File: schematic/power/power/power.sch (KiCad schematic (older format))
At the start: 9 parts

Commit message: full bridge amplifier schematic
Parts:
- removed C? (x2): C, symbol Device:C
- removed Q? (x2): Q_NMOS_GDS, symbol Device:Q_NMOS_GDS
- removed U? (x2): IR21834, symbol Driver_FET:IR21834
- added C1, C2, C5, C6: C, symbol Device:C
- added C? (x2): CP1, symbol Device:CP1
- added D1, D2: DIODE, symbol pspice:DIODE
- added IC1, IC2: NCP5111PG, DIP794W56P254L959H533Q8N, symbol NCP5111PG:NCP5111PG
- added Q3, Q4: Q_NMOS_GDS, symbol Device:Q_NMOS_GDS
- gave numbers to parts that had none: 3
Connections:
- net labels added: +15V, GND, OUT+, OUT-, PWM_IN, VDD
- wire segments 0 -> 74
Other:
- moved on the sheet: Q1, Q2, U1A

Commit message: Added connectors and filter section
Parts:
- removed U1: 74LS04, symbol 74xx:74LS04
- added C? (x3): C, symbol Device:C
- added J? (x2): Conn_01x04_Female, TerminalBlock_TE-Connectivity:TerminalBlock_TE_282834-4_1x04_P2.54mm_Horizontal, symbol Connector:Conn_01x04_Female
- added J?: Conn_01x02_Female, TerminalBlock_TE-Connectivity:TerminalBlock_TE_282834-2_1x02_P2.54mm_Horizontal, symbol Connector:Conn_01x02_Female
- added L? (x2): INDUCTOR, symbol pspice:INDUCTOR
- IC1, IC2: symbol NCP5111PG:NCP5111PG -> power-rescue:NCP5111PG-NCP5111PG
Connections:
- net +15V: now also J?.2 (Pin_2)
- net GND: now also C?.1, C?.1, J?.3 (Pin_3), J?.3 (Pin_3), J?.4 (Pin_4), J?.4 (Pin_4)
- net VDD: now also J?.1 (Pin_1)
- net PWM-: now reaches IC2.2 (IN)
- net PWM-: now also J?.2 (Pin_2)
- net OUT+ renamed P+
- net P+: now also L?.1
- net OUT- renamed P-
- net P-: now also L?.2
- net PWM_IN renamed PWM+
- net PWM+: now also J?.1 (Pin_1)
- new net O+: C?.2, C?.2, J?.1 (Pin_1), L?.2
- new net O-: C?.1, C?.2, J?.2 (Pin_2), L?.1
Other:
- note added: "Filter Section"
- note added: "Power Section"
- moved on the sheet: C1, C2, C5, C6, C?, D1, D2, IC1, IC2, Q1, Q2, Q3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

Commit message: assign part number to power schematic
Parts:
- removed C2, C5, C6, C? (x3): C, symbol Device:C
- removed C?: CP1, symbol Device:CP1
- removed D1, D2: DIODE, symbol pspice:DIODE
- removed IC2: NCP5111PG, DIP794W56P254L959H533Q8N, symbol power-rescue:NCP5111PG-NCP5111PG
- removed J? (x2): Conn_01x04_Female, TerminalBlock_TE-Connectivity:TerminalBlock_TE_282834-4_1x04_P2.54mm_Horizontal, symbol Connector:Conn_01x04_Female
- removed J?: Conn_01x02_Female, TerminalBlock_TE-Connectivity:TerminalBlock_TE_282834-2_1x02_P2.54mm_Horizontal, symbol Connector:Conn_01x02_Female
- removed L? (x2): INDUCTOR, symbol pspice:INDUCTOR
- added C1, C3, C5, C6, C8: ECE-A1HN100U, Capacitor_THT:CP_Radial_D6.3mm_P2.50mm, symbol Device:CP1
- added C7: UKZ1H101MHM1TO, Capacitor_THT:CP_Radial_D12.5mm_P5.00mm, symbol Device:CP1
- added D1, D2: 1N4936, KiCad:DIOAD1405W86L465D235, symbol 1N4936:1N4936
- added IC2: NCP5111PG, NCP5111PG:DIP794W56P254L959H533Q8N, symbol NCP5111PG:NCP5111PG
- added J1, J2: 1935161, TerminalBlock:TerminalBlock_Altech_AK300-2_P5.00mm, symbol Connector_Generic:Conn_01x02
- added R1, R2, R3, R4: CFR-50JB-52-10R, Resistor_THT:R_Axial_DIN0309_L9.0mm_D3.2mm_P12.70mm_Horizontal, symbol Device:R
- added U1: 74LS04, Package_DIP:DIP-14_W7.62mm, symbol 74xx:74LS04
- C2: renamed from C1; value C -> UKZ1H101MHM1TO; footprint (none) -> Capacitor_THT:CP_Radial_D12.5mm_P5.00mm; symbol Device:C -> Device:CP1; Description (none) -> 100uF 50V 20%
- C4: renamed from C?; value CP1 -> ECE-A1HN100U; footprint (none) -> Capacitor_THT:CP_Radial_D6.3mm_P2.50mm; Description (none) -> 10uF 50V 20%
- IC1: footprint DIP794W56P254L959H533Q8N -> NCP5111PG:DIP794W56P254L959H533Q8N; symbol power-rescue:NCP5111PG-NCP5111PG -> NCP5111PG:NCP5111PG
- Q1, Q2, Q3, Q4: value Q_NMOS_GDS -> FQP17N40; footprint (none) -> FQP17N40:TO254P470X990X1910-3P
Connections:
- net +15V: now also C1.1, C7.1, C8.1, D1.2, D2.2, IC2.1 (VCC), J1.2 (Pin_2), U1.14 (VCC)
- net GND: now also C1.2, C5.2, C7.2, C8.2, IC2.3 (GND), J1.1 (Pin_1), J2.1 (Pin_1), U1.7 (GND)
- net VDD: now also C5.1, J2.2 (Pin_2)
- net at IC1.7 (DRV_HI): now also R1.2; no longer Q1.1 (G)
- net at IC1.4 (DRV_LO): now also R2.2; no longer Q2.1 (G)
- net at IC1.8 (VBOOT): now also C3.1, D1.1
- net at Q3.1 (G): now also R3.1
- net at Q4.1 (G): now also R4.1
- net P+ renamed OUT+
- net OUT+: now also C3.2
- net P- renamed OUT-
- net OUT-: now also C6.2, IC2.6 (BRIDGE)
- net PWM+ renamed PWM_IN
- net PWM_IN: now also U1.1
- new net: IC2.2 (IN), U1.2
- new net: Q2.1 (G), R2.1
- new net: IC2.4 (DRV_LO), R4.2
- new net: IC2.7 (DRV_HI), R3.2
- new net: C6.1, D2.1, IC2.8 (VBOOT)
- new net: Q1.1 (G), R1.1
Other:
- note removed: "Filter Section"
- note removed: "Power Section"
- moved on the sheet: C4, IC1

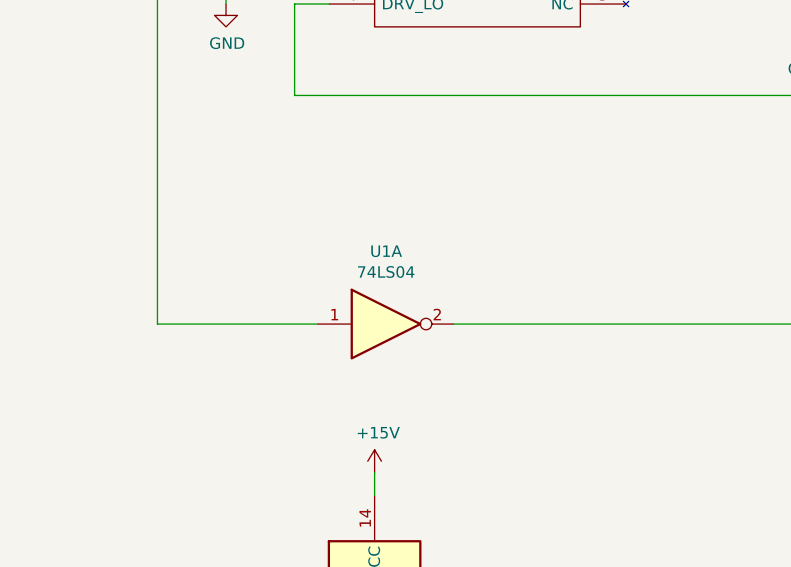
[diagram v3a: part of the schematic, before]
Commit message: initial PCB layout for power
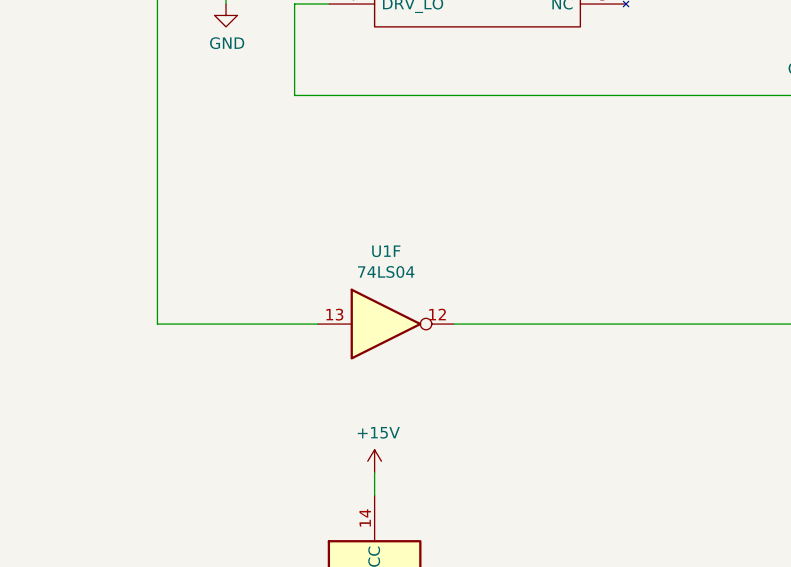
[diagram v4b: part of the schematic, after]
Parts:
- removed unit 1 of U1
- added unit 6 of U1
- D1, D2: footprint KiCad:DIOAD1405W86L465D235 -> 1N4936:DIOAD1405W86L465D235
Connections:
- net PWM_IN: now also U1.13
- net at IC2.2 (IN): now also U1.12
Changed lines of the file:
@@
 $EndDescr
-$Comp
-L 74xx:74LS04 U1
-U 1 1 61124B51
-P 2500 5250
-F 0 "U1" H 2500 5567 50  0000 C CNN
-F 1 "74LS04" H 2500 5476 50  0000 C CNN
-F 2 "Package_DIP:DIP-14_W7.62mm" H 2500 5250 50  0001 C CNN
-F 3 "http://www.ti.com/lit/gpn/sn74LS04" H 2500 5250 50  0001 C CNN
-	1    2500 5250
-	1    0    0    -1
-$EndComp
 $Comp
 L NCP5111PG:NCP5111PG IC1
@@
 F 0 "D1" H 3350 2583 50  0000 C CNN
 F 1 "1N4936" H 3350 2674 50  0000 C CNN
-F 2 "KiCad:DIOAD1405W86L465D235" H 3500 2850 50  0001 L CNN
+F 2 "1N4936:DIOAD1405W86L465D235" H 3500 2850 50  0001 L CNN
 F 3 "http://www.onsemi.com/pub/Collateral/1N4933-D.PDF" H 3500 2750 50  0001 L CNN
 F 4 "ON Semi 1N4936 Switching Diode, 400V 1A, 2-Pin DO-41" H 3500 2650 50  0001 L CNN "Description"
@@
 Wire Wire Line
 	5100 3750 5100 4050
-$Comp
-L 74xx:74LS04 U1
-U 7 1 612F6319
-P 2450 6500
-F 0 "U1" H 2680 6546 50  0000 L CNN
-F 1 "74LS04" H 2680 6455 50  0000 L CNN
-F 2 "Package_DIP:DIP-14_W7.62mm" H 2450 6500 50  0001 C CNN
-F 3 "http://www.ti.com/lit/gpn/sn74LS04" H 2450 6500 50  0001 C CNN
-	7    2450 6500
-	1    0    0    -1
-$EndComp
 $Comp
 L Connector_Generic:Conn_01x02 J2
@@
 Wire Wire Line
 	10250 3200 10250 3250
+Wire Wire Line
+	9450 2850 9200 2850
+Connection ~ 9450 2850
+Wire Wire Line
+	8600 2850 7950 2850
+$Comp
+L Device:R R3
+U 1 1 61215FEE
+P 7100 3350
+F 0 "R3" V 6893 3350 50  0000 C CNN
+F 1 "CFR-50JB-52-10R" V 6984 3350 50  0000 C CNN
+F 2 "Resistor_THT:R_Axial_DIN0309_L9.0mm_D3.2mm_P12.70mm_Horizontal" V 7030 3350 50  0001 C CNN
+F 3 "~" H 7100 3350 50  0001 C CNN
+F 4 "10R 0.5W 5%" V 7100 3350 50  0001 C CNN "Description"
+	1    7100 3350
+	0    -1   1    0
+$EndComp
+Wire Wire Line
+	7350 3350 7250 3350
+Wire Wire Line
+	9550 4250 7250 4250
+Wire Wire Line
+	6950 4250 6850 4250
+Wire Wire Line
+	7450 2600 6550 2600
+Connection ~ 7450 3750
+Wire Wire Line
+	6550 3750 6100 3750
+Wire Wire Line
+	7450 3750 6550 3750
+Connection ~ 6550 3750
+$Comp
+L Device:CP1 C5
+U 1 1 61215FFE
+P 7450 2800
+F 0 "C5" H 7565 2846 50  0000 L CNN
+F 1 "ECE-A1HN100U" H 7565 2755 50  0000 L CNN
+F 2 "Capacitor_THT:CP_Radial_D6.3mm_P2.50mm" H 7450 2800 50  0001 C CNN
+F 3 "~" H 7450 2800 50  0001 C CNN
+F 4 "10uF 50V 20%" H 7450 2800 50  0001 C CNN "Description"
+	1    7450 2800
+	-1   0    0    -1
+$EndComp
+Wire Wire Line
+	6950 3350 6850 3350
+Wire Wire Line
+	6550 3550 6550 3750
+Wire Wire Line
+	6550 3750 6550 4050
+$Comp
+L Device:CP1 C7
+U 1 1 61216015
+P 9850 3050
+F 0 "C7" H 9965 3096 50  0000 L CNN
+F 1 "UKZ1H101MHM1TO" H 9850 2900 50  0000 L CNN
+F 2 "Capacitor_THT:CP_Radial_D12.5mm_P5.00mm" H 9888 2900 50  0001 C CNN
+F 3 "~" H 9850 3050 50  0001 C CNN
+F 4 "100uF 50V 20%" H 9850 3050 50  0001 C CNN "Description"
+	1    9850 3050
+	-1   0    0    -1
+$EndComp
+$Comp
+L Device:CP1 C8
+U 1 1 6121601C
+P 10250 3050
+F 0 "C8" H 10365 3096 50  0000 L CNN
+F 1 "ECE-A1HN100U" H 9800 2900 50  0000 L CNN
+F 2 "Capacitor_THT:CP_Radial_D6.3mm_P2.50mm" H 10250 3050 50  0001 C CNN
+F 3 "~" H 10250 3050 50  0001 C CNN
+F 4 "10uF 50V 20%" H 10250 3050 50  0001 C CNN "Description"
+	1    10250 3050
+	-1   0    0    -1
+$EndComp
+$Comp
+L Device:R R4
+U 1 1 61216023
+P 7100 4250
+F 0 "R4" V 6893 4250 50  0000 C CNN
+F 1 "CFR-50JB-52-10R" V 6984 4250 50  0000 C CNN
+F 2 "Resistor_THT:R_Axial_DIN0309_L9.0mm_D3.2mm_P12.70mm_Horizontal" V 7030 4250 50  0001 C CNN
+F 3 "~" H 7100 4250 50  0001 C CNN
+F 4 "10R 0.5W 5%" V 7100 4250 50  0001 C CNN "Description"
+	1    7100 4250
+	0    -1   1    0
+$EndComp
+$Comp
+L Device:CP1 C6
+U 1 1 6121602A
+P 7700 3550
+F 0 "C6" H 7815 3596 50  0000 L CNN
+F 1 "ECE-A1HN100U" H 7815 3505 50  0000 L CNN
+F 2 "Capacitor_THT:CP_Radial_D6.3mm_P2.50mm" H 7700 3550 50  0001 C CNN
+F 3 "~" H 7700 3550 50  0001 C CNN
+F 4 "10uF 50V 20%" H 7700 3550 50  0001 C CNN "Description"
+	1    7700 3550
+	0    1    -1   0
+$EndComp
+Wire Wire Line
+	10150 5250 2800 5250
+Wire Wire Line
+	5800 4750 5800 4700
+Connection ~ 5800 4700
+Wire Wire Line
+	5800 4700 6550 4700
+Text GLabel 5350 3750 2    50   Input ~ 0
+OUT+
+Text GLabel 6100 3750 0    50   Input ~ 0
+OUT-
+$Comp
+L Device:Q_NMOS_GDS Q2
+U 1 1 612588AF
+P 5000 4250
+F 0 "Q2" H 5204 4296 50  0000 L CNN
+F 1 "FQP17N40" H 5204 4205 50  0000 L CNN
+F 2 "FQP17N40:TO254P470X990X1910-3P" H 5200 4350 50  0001 C CNN
+F 3 "~" H 5000 4250 50  0001 C CNN
+	1    5000 4250
+	1    0    0    -1
+$EndComp
+Wire Wire Line
+	6550 2600 6550 3150
+$Comp
+L Device:Q_NMOS_GDS Q3
+U 1 1 612593F2
+P 6650 3350
+F 0 "Q3" H 6854 3396 50  0000 L CNN
+F 1 "FQP17N40" H 6854 3305 50  0000 L CNN
+F 2 "FQP17N40:TO254P470X990X1910-3P" H 6850 3450 50  0001 C CNN
+F 3 "~" H 6650 3350 50  0001 C CNN
+	1    6650 3350
+	-1   0    0    -1
+$EndComp
+$Comp
+L Device:Q_NMOS_GDS Q4
+U 1 1 61266951
+P 6650 4250
+F 0 "Q4" H 6854 4296 50  0000 L CNN
+F 1 "FQP17N40" H 6854 4205 50  0000 L CNN
+F 2 "FQP17N40:TO254P470X990X1910-3P" H 6850 4350 50  0001 C CNN
+F 3 "~" H 6650 4250 50  0001 C CNN
+	1    6650 4250
+	-1   0    0    -1
+$EndComp
 $Comp
 L 1N4936:1N4936 D2
-U 1 1 61215FE4
+U 1 1 6127115C
 P 8600 2850
 F 0 "D2" H 8900 2583 50  0000 C CNN
 F 1 "1N4936" H 8900 2674 50  0000 C CNN
-F 2 "KiCad:DIOAD1405W86L465D235" H 9050 2850 50  0001 L CNN
+F 2 "1N4936:DIOAD1405W86L465D235" H 9050 2850 50  0001 L CNN
 F 3 "http://www.onsemi.com/pub/Collateral/1N4933-D.PDF" H 9050 2750 50  0001 L CNN
 F 4 "ON Semi 1N4936 Switching Diode, 400V 1A, 2-Pin DO-41" H 9050 2650 50  0001 L CNN "Description"
@@
 	1    0    0    1
 $EndComp
-Wire Wire Line
-	9450 2850 9200 2850
-Connection ~ 9450 2850
-Wire Wire Line
-	8600 2850 7950 2850
-$Comp
-L Device:R R3
-U 1 1 61215FEE
-P 7100 3350
-F 0 "R3" V 6893 3350 50  0000 C CNN
-F 1 "CFR-50JB-52-10R" V 6984 3350 50  0000 C CNN
-F 2 "Resistor_THT:R_Axial_DIN0309_L9.0mm_D3.2mm_P12.70mm_Horizontal" V 7030 3350 50  0001 C CNN
-F 3 "~" H 7100 3350 50  0001 C CNN
-F 4 "10R 0.5W 5%" V 7100 3350 50  0001 C CNN "Description"
-	1    7100 3350
-	0    -1   1    0
-$EndComp
-Wire Wire Line
-	7350 3350 7250 3350
-Wire Wire Line
-	9550 4250 7250 4250
-Wire Wire Line
-	6950 4250 6850 4250
-Wire Wire Line
-	7450 2600 6550 2600
-Connection ~ 7450 3750
-Wire Wire Line
-	6550 3750 6100 3750
-Wire Wire Line
-	7450 3750 6550 3750
-Connection ~ 6550 3750
-$Comp
-L Device:CP1 C5
-U 1 1 61215FFE
-P 7450 2800
-F 0 "C5" H 7565 2846 50  0000 L CNN
-F 1 "ECE-A1HN100U" H 7565 2755 50  0000 L CNN
-F 2 "Capacitor_THT:CP_Radial_D6.3mm_P2.50mm" H 7450 2800 50  0001 C CNN
-F 3 "~" H 7450 2800 50  0001 C CNN
-F 4 "10uF 50V 20%" H 7450 2800 50  0001 C CNN "Description"
-	1    7450 2800
-	-1   0    0    -1
-$EndComp
-Wire Wire Line
-	6950 3350 6850 3350
-Wire Wire Line
-	6550 3550 6550 3750
-Wire Wire Line
-	6550 3750 6550 4050
-$Comp
-L Device:CP1 C7
-U 1 1 61216015
-P 9850 3050
-F 0 "C7" H 9965 3096 50  0000 L CNN
-F 1 "UKZ1H101MHM1TO" H 9850 2900 50  0000 L CNN
-F 2 "Capacitor_THT:CP_Radial_D12.5mm_P5.00mm" H 9888 2900 50  0001 C CNN
-F 3 "~" H 9850 3050 50  0001 C CNN
-F 4 "100uF 50V 20%" H 9850 3050 50  0001 C CNN "Description"
-	1    9850 3050
-	-1   0    0    -1
-$EndComp
-$Comp
-L Device:CP1 C8
-U 1 1 6121601C
-P 10250 3050
-F 0 "C8" H 10365 3096 50  0000 L CNN
-F 1 "ECE-A1HN100U" H 9800 2900 50  0000 L CNN
-F 2 "Capacitor_THT:CP_Radial_D6.3mm_P2.50mm" H 10250 3050 50  0001 C CNN
-F 3 "~" H 10250 3050 50  0001 C CNN
-F 4 "10uF 50V 20%" H 10250 3050 50  0001 C CNN "Description"
-	1    10250 3050
-	-1   0    0    -1
-$EndComp
-$Comp
-L Device:R R4
-U 1 1 61216023
-P 7100 4250
-F 0 "R4" V 6893 4250 50  0000 C CNN
-F 1 "CFR-50JB-52-10R" V 6984 4250 50  0000 C CNN
-F 2 "Resistor_THT:R_Axial_DIN0309_L9.0mm_D3.2mm_P12.70mm_Horizontal" V 7030 4250 50  0001 C CNN
-F 3 "~" H 7100 4250 50  0001 C CNN
-F 4 "10R 0.5W 5%" V 7100 4250 50  0001 C CNN "Description"
-	1    7100 4250
-	0    -1   1    0
-$EndComp
-$Comp
-L Device:CP1 C6
-U 1 1 6121602A
-P 7700 3550
-F 0 "C6" H 7815 3596 50  0000 L CNN
-F 1 "ECE-A1HN100U" H 7815 3505 50  0000 L CNN
-F 2 "Capacitor_THT:CP_Radial_D6.3mm_P2.50mm" H 7700 3550 50  0001 C CNN
-F 3 "~" H 7700 3550 50  0001 C CNN
-F 4 "10uF 50V 20%" H 7700 3550 50  0001 C CNN "Description"
-	1    7700 3550
-	0    1    -1   0
-$EndComp
-Wire Wire Line
-	10150 5250 2800 5250
-Wire Wire Line
-	5800 4750 5800 4700
-Connection ~ 5800 4700
-Wire Wire Line
-	5800 4700 6550 4700
-Text GLabel 5350 3750 2    50   Input ~ 0
-OUT+
-Text GLabel 6100 3750 0    50   Input ~ 0
-OUT-
-$Comp
-L Device:Q_NMOS_GDS Q2
-U 1 1 612588AF
-P 5000 4250
-F 0 "Q2" H 5204 4296 50  0000 L CNN
-F 1 "FQP17N40" H 5204 4205 50  0000 L CNN
-F 2 "FQP17N40:TO254P470X990X1910-3P" H 5200 4350 50  0001 C CNN
-F 3 "~" H 5000 4250 50  0001 C CNN
-	1    5000 4250
-	1    0    0    -1
-$EndComp
-Wire Wire Line
-	6550 2600 6550 3150
-$Comp
-L Device:Q_NMOS_GDS Q3
-U 1 1 612593F2
-P 6650 3350
-F 0 "Q3" H 6854 3396 50  0000 L CNN
-F 1 "FQP17N40" H 6854 3305 50  0000 L CNN
-F 2 "FQP17N40:TO254P470X990X1910-3P" H 6850 3450 50  0001 C CNN
-F 3 "~" H 6650 3350 50  0001 C CNN
-	1    6650 3350
-	-1   0    0    -1
-$EndComp
-$Comp
-L Device:Q_NMOS_GDS Q4
-U 1 1 61266951
-P 6650 4250
-F 0 "Q4" H 6854 4296 50  0000 L CNN
-F 1 "FQP17N40" H 6854 4205 50  0000 L CNN
-F 2 "FQP17N40:TO254P470X990X1910-3P" H 6850 4350 50  0001 C CNN
-F 3 "~" H 6650 4250 50  0001 C CNN
-	1    6650 4250
-	-1   0    0    -1
+$Comp
+L 74xx:74LS04 U1
+U 7 1 612F6319
+P 2450 6500
+F 0 "U1" H 2680 6546 50  0000 L CNN
+F 1 "74LS04" H 2680 6455 50  0000 L CNN
+F 2 "Package_DIP:DIP-14_W7.62mm" H 2450 6500 50  0001 C CNN
+F 3 "http://www.ti.com/lit/gpn/sn74LS04" H 2450 6500 50  0001 C CNN
+	7    2450 6500
+	1    0    0    -1
+$EndComp
+$Comp
+L 74xx:74LS04 U1
+U 6 1 6128A88A
+P 2500 5250
+F 0 "U1" H 2500 5567 50  0000 C CNN
+F 1 "74LS04" H 2500 5476 50  0000 C CNN
+F 2 "Package_DIP:DIP-14_W7.62mm" H 2500 5250 50  0001 C CNN
+F 3 "http://www.ti.com/lit/gpn/sn74LS04" H 2500 5250 50  0001 C CNN
+	6    2500 5250
+	1    0    0    -1
 $EndComp
 $EndSCHEMATC

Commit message: add power ver 2
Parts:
- removed unit 6 of U1
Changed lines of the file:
@@
-	1    0    0    -1
-$EndComp
-$Comp
-L 74xx:74LS04 U1
-U 6 1 6128A88A
-P 2500 5250
-F 0 "U1" H 2500 5567 50  0000 C CNN
-F 1 "74LS04" H 2500 5476 50  0000 C CNN
-F 2 "Package_DIP:DIP-14_W7.62mm" H 2500 5250 50  0001 C CNN
-F 3 "http://www.ti.com/lit/gpn/sn74LS04" H 2500 5250 50  0001 C CNN
-	6    2500 5250
 	1    0    0    -1
 $EndComp
